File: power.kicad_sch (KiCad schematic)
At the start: 38 parts, among them U7 MAX77827AEFD+T, U8 SC4215

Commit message: 2nd iteration to be reviewed
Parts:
- removed C? (x3): 0.1uF, Capacitor_SMD:C_0402_1005Metric, symbol Device:C_Small
- removed H? (x4): MountingHole_Pad, MountingHole:MountingHole_3.2mm_M3_DIN965_Pad, symbol Mechanical:MountingHole_Pad
- removed Q? (x2): SI4143DY-T1-GE3, Package_SO:SOIC-8_3.9x4.9mm_P1.27mm, symbol Device:Q_PMOS_GDS
- removed TP5, TP6, TP7: TestPoint, TestPoint:TestPoint_Pad_D1.5mm, symbol Connector:TestPoint
- removed U?: XC8111, Package_TO_SOT_SMD:SOT-23-5, symbol Analog_Switch:MAX40200AUK
- removed U? (x2): LTC4412xS6, Package_TO_SOT_SMD:TSOT-23-6, symbol Power_Management:LTC4412xS6
- added TP9: TestPoint, TestPoint:TestPoint_Pad_D1.5mm, symbol Connector:TestPoint
- J4: renamed from J?; footprint (none) -> Connector_PinHeader_2.54mm:PinHeader_1x02_P2.54mm_Vertical
- gave numbers to parts that had none: 6
- renumbered C23 to C27, C25 to C29, C26 to C30, C27 to C31, C28 to C32, C29 to C33, C30 to C34, C31 to C35, R16 to R17, R17 to R18, R18 to R19, TP4 to TP6, U7 to U10, U8 to U11
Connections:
- net +3V3: now also C34.2, C35.2, R18.1, U11.6 (VOUT), TP9.1
- no-connect marks 5 -> 4
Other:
- moved on the sheet: C27

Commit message: spaced out vias and changed j4
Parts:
- J4: footprint Connector_PinHeader_2.54mm:PinHeader_1x02_P2.54mm_Vertical -> Connector_JST:JST_PH_B2B-PH-K_1x02_P2.00mm_Vertical
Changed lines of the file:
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@@
       (effects (font (size 1.27 1.27)))
     )
-    (property "Footprint" "Connector_PinHeader_2.54mm:PinHeader_1x02_P2.54mm_Vertical" (at 31.75 87.63 0)
+    (property "Footprint" "Connector_JST:JST_PH_B2B-PH-K_1x02_P2.00mm_Vertical" (at 31.75 87.63 0)
       (effects (font (size 1.27 1.27)) hide)
     )

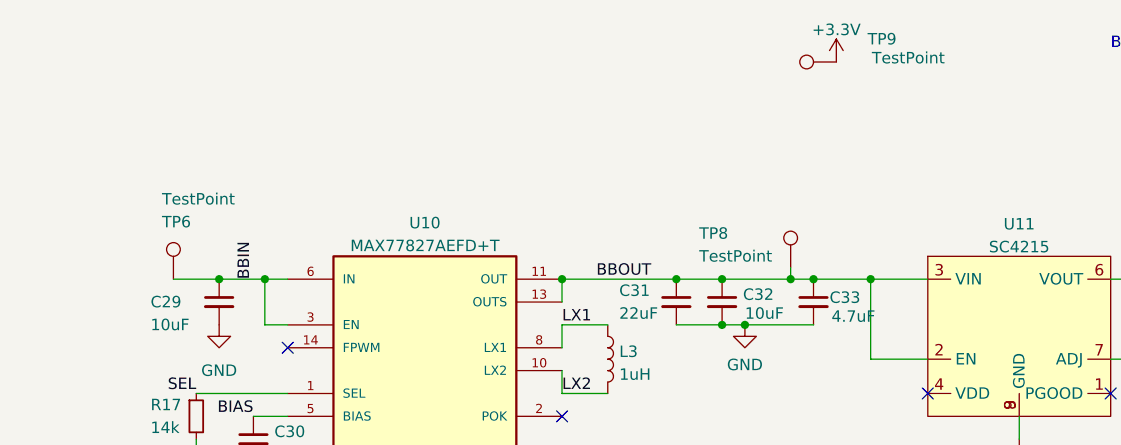
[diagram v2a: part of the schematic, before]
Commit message: rerouted spi bus and changed NAND
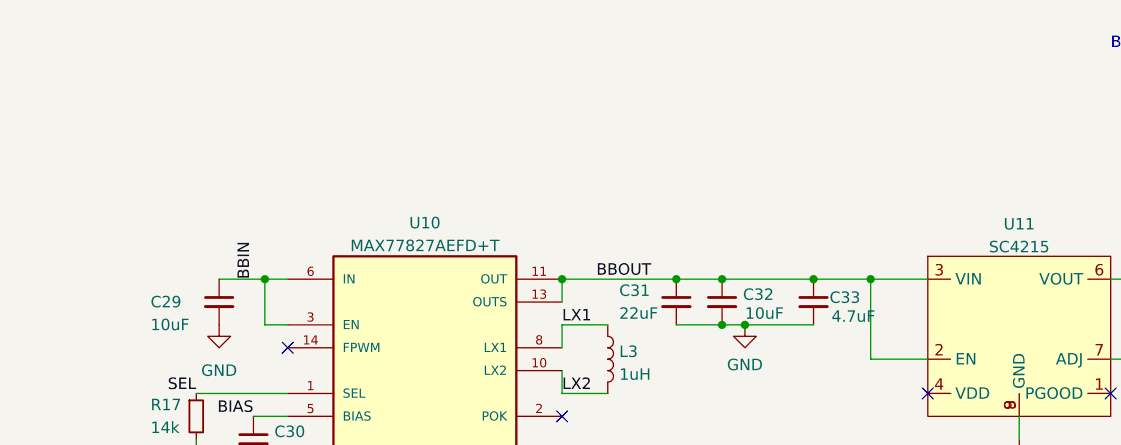
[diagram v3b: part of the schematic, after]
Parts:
- removed TP6, TP8, TP9: TestPoint, TestPoint:TestPoint_Pad_D1.5mm, symbol Connector:TestPoint
